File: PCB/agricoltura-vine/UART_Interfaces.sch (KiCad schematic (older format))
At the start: 8 parts, among them T4 BM04B-SRSS-TB(LF)(SN), T5 BM04B-SRSS-TB(LF)(SN), T6 BM04B-SRSS-TB(LF)(SN), T7 BM04B-SRSS-TB(LF)(SN), U2 74HC4052D

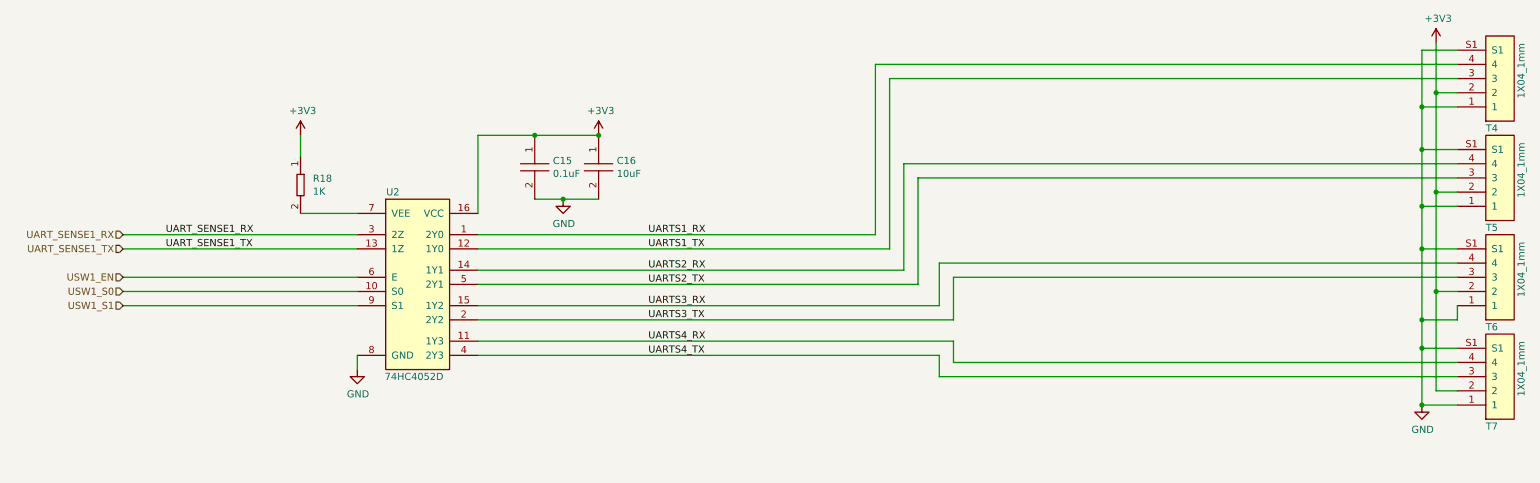
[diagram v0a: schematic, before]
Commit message: TVS Diodes
TVS diodes and pullups added to sensor connectors, implemented in schematic and board.
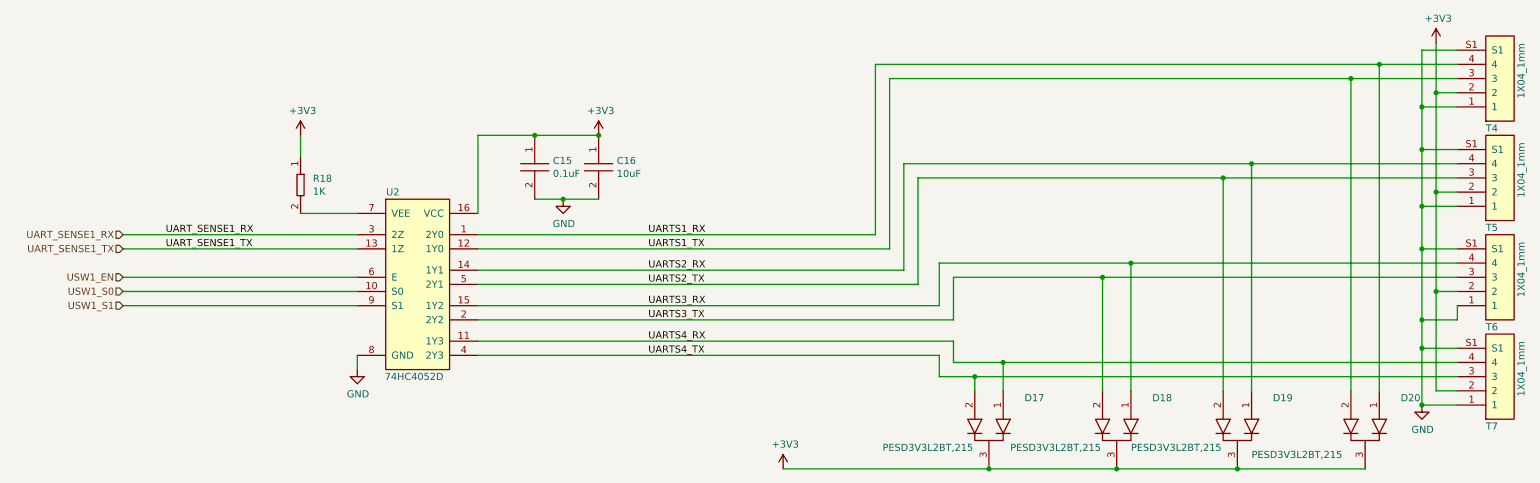
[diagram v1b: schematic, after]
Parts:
- added D17, D18, D19, D20: PESD3V3L2BT,215, AVR-KiCAD-Lib-Diodes:SOT-23, symbol AVR-KiCAD-Lib-Diodes:PESD3V3L2BT,215
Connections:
- net +3V3: now also D17.3, D18.3, D19.3, D20.3
- net UARTS1_RX: now also D20.1
- net UARTS1_TX: now also D20.2
- net UARTS2_RX: now also D19.1
- net UARTS2_TX: now also D19.2
- net UARTS3_RX: now also D18.1
- net UARTS3_TX: now also D18.2
- net UARTS4_RX: now also D17.1
- net UARTS4_TX: now also D17.2
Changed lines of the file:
@@
 	10450 4600 10450 3900
 Wire Wire Line
-	6500 2300 10600 2300
+	6500 2300 10050 2300
 Wire Wire Line
 	6500 2300 6500 3500
 Wire Wire Line
-	6600 2400 10600 2400
+	6600 2400 9850 2400
 Wire Wire Line
 	6600 2400 6600 3600
 Wire Wire Line
-	6700 3000 10600 3000
+	6700 3000 9150 3000
 Wire Wire Line
 	6700 3000 6700 3750
 Wire Wire Line
-	10600 3100 6800 3100
+	10600 3100 8950 3100
 Wire Wire Line
 	6800 3100 6800 3850
 Wire Wire Line
-	10600 3700 6950 3700
+	10600 3700 8300 3700
 Wire Wire Line
 	6950 3700 6950 4000
@@
 	7050 4100 7050 3800
 Wire Wire Line
-	7050 3800 10600 3800
+	7050 3800 8100 3800
 Wire Wire Line
 	7050 4250 7050 4400
 Wire Wire Line
-	7050 4400 10600 4400
+	7050 4400 7400 4400
 Wire Wire Line
 	3700 4250 7050 4250
 Wire Wire Line
-	10600 4500 6950 4500
+	10600 4500 7200 4500
 Wire Wire Line
 	6950 4500 6950 4350
@@
 Wire Wire Line
 	2450 3350 2850 3350
+$Comp
+L AVR-KiCAD-Lib-Diodes:PESD3V3L2BT,215 D?
+U 1 1 5F44F9D9
+P 7300 4850
+AR Path="/5EE827B2/5F44F9D9" Ref="D?"  Part="1"
+AR Path="/5EE82702/5F44F9D9" Ref="D17"  Part="1"
+F 0 "D17" V 7100 5100 50  0000 L CNN
+F 1 "PESD3V3L2BT,215" H 7350 5050 50  0001 C CNN
+F 2 "AVR-KiCAD-Lib-Diodes:SOT-23" H 7200 4850 50  0001 C CNN
+F 3 "https://assets.nexperia.com/documents/data-sheet/PESDXL2BT_SER.pdf" H 7200 4950 50  0001 C CNN
+F 4 "0.45000" H 7400 5100 50  0001 C CNN "Cost QTY: 1"
+F 5 "0.13260" H 7500 5200 50  0001 C CNN "Cost QTY: 1000"
+F 6 "*" H 7600 5300 50  0001 C CNN "Cost QTY: 2500"
+F 7 "*" H 7700 5400 50  0001 C CNN "Cost QTY: 5000"
+F 8 "*" H 7800 5500 50  0001 C CNN "Cost QTY: 10000"
+F 9 "Nexperia USA Inc." H 7900 5600 50  0001 C CNN "MFR"
+F 10 "PESD3V3L2BT,215" H 8000 5700 50  0001 C CNN "MFR#"
+F 11 "Digikey" H 8100 5800 50  0001 C CNN "Vendor"
+F 12 "1727-3826-1-ND" H 8200 5900 50  0001 C CNN "Vendor #"
+F 13 "AVR" H 8300 6000 50  0001 C CNN "Designer"
+F 14 "1.1mm" H 8400 6100 50  0001 C CNN "Height"
+F 15 "6/15/2020" H 9500 7200 50  0001 C CNN "Date Created"
+F 16 "6/15/2020" H 8500 6200 50  0001 C CNN "Date Modified"
+F 17 "Yes" H 8600 6300 50  0001 C CNN "Lead-Free ?"
+F 18 "1" H 8700 6400 50  0001 C CNN "RoHS Levels"
+F 19 "SMT" H 8800 6500 50  0001 C CNN "Mounting"
+F 20 "3" H 8900 6600 50  0001 C CNN "Pin Count #"
+F 21 "Active" H 9000 6700 50  0001 C CNN "Status"
+F 22 "*" H 9100 6800 50  0001 C CNN "Tolerance"
+F 23 "TVS" H 9200 6900 50  0001 C CNN "Type"
+F 24 "*" H 9300 7000 50  0001 C CNN "Voltage"
+F 25 " SOT-23-3" H 9400 7150 50  0001 C CNN "Package"
+F 26 "26V Clamp 15A (8/20µs) Ipp Tvs Diode Surface Mount TO-236AB" H 9700 7450 50  0001 C CNN "Description"
+F 27 "PESD3V3L2BT,215" V 7450 4100 50  0000 L CNN "_Value_"
+F 28 "*" H 9700 7450 50  0001 C CNN "Management_ID"
+	1    7300 4850
+	0    1    1    0
+$EndComp
+$Comp
+L AVR-KiCAD-Lib-Diodes:PESD3V3L2BT,215 D?
+U 1 1 5F45133E
+P 8200 4850
+AR Path="/5EE827B2/5F45133E" Ref="D?"  Part="1"
+AR Path="/5EE82702/5F45133E" Ref="D18"  Part="1"
+F 0 "D18" V 8000 5100 50  0000 L CNN
+F 1 "PESD3V3L2BT,215" H 8250 5050 50  0001 C CNN
+F 2 "AVR-KiCAD-Lib-Diodes:SOT-23" H 8100 4850 50  0001 C CNN
+F 3 "https://assets.nexperia.com/documents/data-sheet/PESDXL2BT_SER.pdf" H 8100 4950 50  0001 C CNN
+F 4 "0.45000" H 8300 5100 50  0001 C CNN "Cost QTY: 1"
+F 5 "0.13260" H 8400 5200 50  0001 C CNN "Cost QTY: 1000"
+F 6 "*" H 8500 5300 50  0001 C CNN "Cost QTY: 2500"
+F 7 "*" H 8600 5400 50  0001 C CNN "Cost QTY: 5000"
+F 8 "*" H 8700 5500 50  0001 C CNN "Cost QTY: 10000"
+F 9 "Nexperia USA Inc." H 8800 5600 50  0001 C CNN "MFR"
+F 10 "PESD3V3L2BT,215" H 8900 5700 50  0001 C CNN "MFR#"
+F 11 "Digikey" H 9000 5800 50  0001 C CNN "Vendor"
+F 12 "1727-3826-1-ND" H 9100 5900 50  0001 C CNN "Vendor #"
+F 13 "AVR" H 9200 6000 50  0001 C CNN "Designer"
+F 14 "1.1mm" H 9300 6100 50  0001 C CNN "Height"
+F 15 "6/15/2020" H 10400 7200 50  0001 C CNN "Date Created"
+F 16 "6/15/2020" H 9400 6200 50  0001 C CNN "Date Modified"
+F 17 "Yes" H 9500 6300 50  0001 C CNN "Lead-Free ?"
+F 18 "1" H 9600 6400 50  0001 C CNN "RoHS Levels"
+F 19 "SMT" H 9700 6500 50  0001 C CNN "Mounting"
+F 20 "3" H 9800 6600 50  0001 C CNN "Pin Count #"
+F 21 "Active" H 9900 6700 50  0001 C CNN "Status"
+F 22 "*" H 10000 6800 50  0001 C CNN "Tolerance"
+F 23 "TVS" H 10100 6900 50  0001 C CNN "Type"
+F 24 "*" H 10200 7000 50  0001 C CNN "Voltage"
+F 25 " SOT-23-3" H 10300 7150 50  0001 C CNN "Package"
+F 26 "26V Clamp 15A (8/20µs) Ipp Tvs Diode Surface Mount TO-236AB" H 10600 7450 50  0001 C CNN "Description"
+F 27 "PESD3V3L2BT,215" V 8350 4100 50  0000 L CNN "_Value_"
+F 28 "*" H 10600 7450 50  0001 C CNN "Management_ID"
+	1    8200 4850
+	0    1    1    0
+$EndComp
+$Comp
+L AVR-KiCAD-Lib-Diodes:PESD3V3L2BT,215 D?
+U 1 1 5F45308D
+P 9050 4850
+AR Path="/5EE827B2/5F45308D" Ref="D?"  Part="1"
+AR Path="/5EE82702/5F45308D" Ref="D19"  Part="1"
+F 0 "D19" V 8850 5100 50  0000 L CNN
+F 1 "PESD3V3L2BT,215" H 9100 5050 50  0001 C CNN
+F 2 "AVR-KiCAD-Lib-Diodes:SOT-23" H 8950 4850 50  0001 C CNN
+F 3 "https://assets.nexperia.com/documents/data-sheet/PESDXL2BT_SER.pdf" H 8950 4950 50  0001 C CNN
+F 4 "0.45000" H 9150 5100 50  0001 C CNN "Cost QTY: 1"
+F 5 "0.13260" H 9250 5200 50  0001 C CNN "Cost QTY: 1000"
+F 6 "*" H 9350 5300 50  0001 C CNN "Cost QTY: 2500"
+F 7 "*" H 9450 5400 50  0001 C CNN "Cost QTY: 5000"
+F 8 "*" H 9550 5500 50  0001 C CNN "Cost QTY: 10000"
+F 9 "Nexperia USA Inc." H 9650 5600 50  0001 C CNN "MFR"
+F 10 "PESD3V3L2BT,215" H 9750 5700 50  0001 C CNN "MFR#"
+F 11 "Digikey" H 9850 5800 50  0001 C CNN "Vendor"
+F 12 "1727-3826-1-ND" H 9950 5900 50  0001 C CNN "Vendor #"
+F 13 "AVR" H 10050 6000 50  0001 C CNN "Designer"
+F 14 "1.1mm" H 10150 6100 50  0001 C CNN "Height"
+F 15 "6/15/2020" H 11250 7200 50  0001 C CNN "Date Created"
+F 16 "6/15/2020" H 10250 6200 50  0001 C CNN "Date Modified"
+F 17 "Yes" H 10350 6300 50  0001 C CNN "Lead-Free ?"
+F 18 "1" H 10450 6400 50  0001 C CNN "RoHS Levels"
+F 19 "SMT" H 10550 6500 50  0001 C CNN "Mounting"
+F 20 "3" H 10650 6600 50  0001 C CNN "Pin Count #"
+F 21 "Active" H 10750 6700 50  0001 C CNN "Status"
+F 22 "*" H 10850 6800 50  0001 C CNN "Tolerance"
+F 23 "TVS" H 10950 6900 50  0001 C CNN "Type"
+F 24 "*" H 11050 7000 50  0001 C CNN "Voltage"
+F 25 " SOT-23-3" H 11150 7150 50  0001 C CNN "Package"
+F 26 "26V Clamp 15A (8/20µs) Ipp Tvs Diode Surface Mount TO-236AB" H 11450 7450 50  0001 C CNN "Description"
+F 27 "PESD3V3L2BT,215" V 9200 4100 50  0000 L CNN "_Value_"
+F 28 "*" H 11450 7450 50  0001 C CNN "Management_ID"
+	1    9050 4850
+	0    1    1    0
+$EndComp
+$Comp
+L AVR-KiCAD-Lib-Diodes:PESD3V3L2BT,215 D?
+U 1 1 5F454162
+P 9950 4850
+AR Path="/5EE827B2/5F454162" Ref="D?"  Part="1"
+AR Path="/5EE82702/5F454162" Ref="D20"  Part="1"
+F 0 "D20" V 9750 5100 50  0000 L CNN
+F 1 "PESD3V3L2BT,215" H 10000 5050 50  0001 C CNN
+F 2 "AVR-KiCAD-Lib-Diodes:SOT-23" H 9850 4850 50  0001 C CNN
+F 3 "https://assets.nexperia.com/documents/data-sheet/PESDXL2BT_SER.pdf" H 9850 4950 50  0001 C CNN
+F 4 "0.45000" H 10050 5100 50  0001 C CNN "Cost QTY: 1"
+F 5 "0.13260" H 10150 5200 50  0001 C CNN "Cost QTY: 1000"
+F 6 "*" H 10250 5300 50  0001 C CNN "Cost QTY: 2500"
+F 7 "*" H 10350 5400 50  0001 C CNN "Cost QTY: 5000"
+F 8 "*" H 10450 5500 50  0001 C CNN "Cost QTY: 10000"
+F 9 "Nexperia USA Inc." H 10550 5600 50  0001 C CNN "MFR"
+F 10 "PESD3V3L2BT,215" H 10650 5700 50  0001 C CNN "MFR#"
+F 11 "Digikey" H 10750 5800 50  0001 C CNN "Vendor"
+F 12 "1727-3826-1-ND" H 10850 5900 50  0001 C CNN "Vendor #"
+F 13 "AVR" H 10950 6000 50  0001 C CNN "Designer"
+F 14 "1.1mm" H 11050 6100 50  0001 C CNN "Height"
+F 15 "6/15/2020" H 12150 7200 50  0001 C CNN "Date Created"
+F 16 "6/15/2020" H 11150 6200 50  0001 C CNN "Date Modified"
+F 17 "Yes" H 11250 6300 50  0001 C CNN "Lead-Free ?"
+F 18 "1" H 11350 6400 50  0001 C CNN "RoHS Levels"
+F 19 "SMT" H 11450 6500 50  0001 C CNN "Mounting"
+F 20 "3" H 11550 6600 50  0001 C CNN "Pin Count #"
+F 21 "Active" H 11650 6700 50  0001 C CNN "Status"
+F 22 "*" H 11750 6800 50  0001 C CNN "Tolerance"
+F 23 "TVS" H 11850 6900 50  0001 C CNN "Type"
+F 24 "*" H 11950 7000 50  0001 C CNN "Voltage"
+F 25 " SOT-23-3" H 12050 7150 50  0001 C CNN "Package"
+F 26 "26V Clamp 15A (8/20µs) Ipp Tvs Diode Surface Mount TO-236AB" H 12350 7450 50  0001 C CNN "Description"
+F 27 "PESD3V3L2BT,215" V 10150 4050 50  0000 L CNN "_Value_"
+F 28 "*" H 12350 7450 50  0001 C CNN "Management_ID"
+	1    9950 4850
+	0    1    1    0
+$EndComp
+Connection ~ 8200 5150
+Wire Wire Line
+	8200 5150 9050 5150
+Connection ~ 9050 5150
+Wire Wire Line
+	9050 5150 9950 5150
+$Comp
+L power:+3V3 #PWR?
+U 1 1 5F461500
+P 5850 5150
+AR Path="/5EE82896/5F461500" Ref="#PWR?"  Part="1"
+AR Path="/5EE82702/5F461500" Ref="#PWR0141"  Part="1"
+F 0 "#PWR0141" H 5850 5000 50  0001 C CNN
+F 1 "+3V3" H 5865 5323 50  0000 C CNN
+F 2 "" H 5850 5150 50  0001 C CNN
+F 3 "" H 5850 5150 50  0001 C CNN
+	1    5850 5150
+	1    0    0    -1
+$EndComp
+Wire Wire Line
+	7200 4600 7200 4500
+Connection ~ 7200 4500
+Wire Wire Line
+	7200 4500 6950 4500
+Wire Wire Line
+	7400 4600 7400 4400
+Connection ~ 7400 4400
+Wire Wire Line
+	7400 4400 10600 4400
+Wire Wire Line
+	8100 4600 8100 3800
+Connection ~ 8100 3800
+Wire Wire Line
+	8100 3800 10600 3800
+Wire Wire Line
+	8300 4600 8300 3700
+Connection ~ 8300 3700
+Wire Wire Line
+	8300 3700 6950 3700
+Wire Wire Line
+	8950 4600 8950 3100
+Connection ~ 8950 3100
+Wire Wire Line
+	8950 3100 6800 3100
+Wire Wire Line
+	9150 4600 9150 3000
+Connection ~ 9150 3000
+Wire Wire Line
+	9150 3000 10600 3000
+Wire Wire Line
+	9850 4600 9850 2400
+Connection ~ 9850 2400
+Wire Wire Line
+	9850 2400 10600 2400
+Wire Wire Line
+	10050 4600 10050 2300
+Connection ~ 10050 2300
+Wire Wire Line
+	10050 2300 10600 2300
+Wire Wire Line
+	5850 5150 7300 5150
+Connection ~ 7300 5150
+Wire Wire Line
+	7300 5150 8200 5150
 $EndSCHEMATC
